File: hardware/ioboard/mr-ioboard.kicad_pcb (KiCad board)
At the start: 4 copper layers, 65 x 80 mm, 131 parts, among them J1 Conn_01x40_Shielded, J2 USB_C_Receptacle_USB2.0, J3 Conn_01x06, J4 Micro_SD_Card_Det, J5 Conn_01x04, J6 Conn_01x02, Q1 2N7002, SW1 SW_Push, U1 TPS62822, U10 F1C200S, U11 TPS54202DDC, U2 TPS56637, U3 TPD2E2U06, U4 DS90C363, U5 TPD2E2U06, U6 LD3985M28R_SOT23, U7 TPS62822, U8 FUSB302BMPX, U9 TPD2E2U06, Y1 24MHz

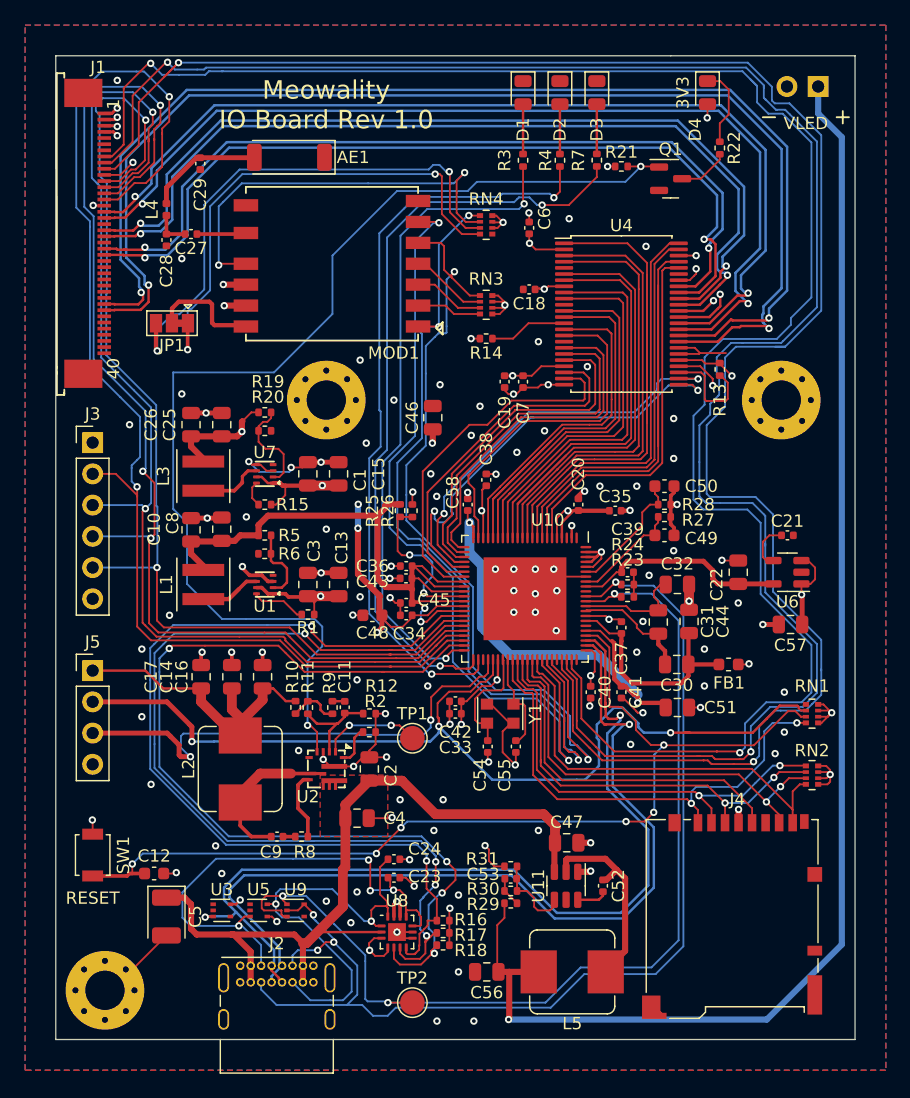
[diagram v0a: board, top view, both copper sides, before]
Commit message: Add LRADC buttons to IO board
Signed-off-by: gatecat <gatecat@ds0.me>
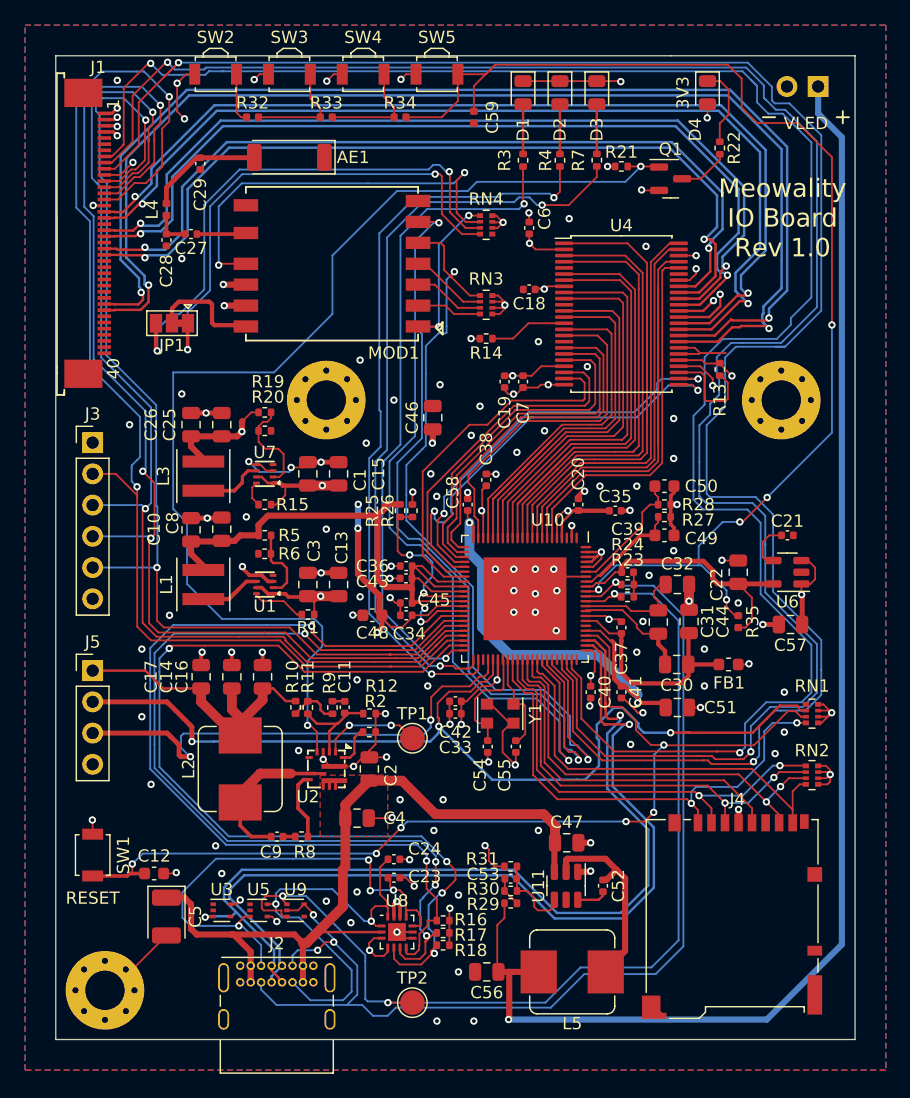
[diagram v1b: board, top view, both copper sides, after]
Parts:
- added C59: 100n, Capacitor_SMD:C_0402_1005Metric, F.Cu at (134.0, 55.0)
- added R32: 2.2k, Resistor_SMD:R_0402_1005Metric, F.Cu at (116.0, 55.0)
- added R33: 2.2k, Resistor_SMD:R_0402_1005Metric, F.Cu at (122.0, 55.0)
- added R34: 2.2k, Resistor_SMD:R_0402_1005Metric, F.Cu at (128.0, 55.0)
- added R35: 2.2k, Resistor_SMD:R_0402_1005Metric, F.Cu at (155.5, 96.0)
- added SW2: SW_Push, Button_Switch_SMD:SW_SPST_B3U-3000P, F.Cu at (113.0, 51.5)
- added SW3: SW_Push, Button_Switch_SMD:SW_SPST_B3U-3000P, F.Cu at (119.0, 51.5)
- added SW4: SW_Push, Button_Switch_SMD:SW_SPST_B3U-3000P, F.Cu at (125.0, 51.5)
- added SW5: SW_Push, Button_Switch_SMD:SW_SPST_B3U-3000P, F.Cu at (131.0, 51.5)
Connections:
- U10 pad 79: unconnected-(U10-Pad79) -> /LRADC
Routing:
- net /LRADC: track 0.00 -> 101.3 mm, vias 0 -> 5
- net GND: track 132.3 -> 150.8 mm, vias 121 -> 128
- net Net-(R33-Pad2): track 0.00 -> 8.87 mm
- net Net-(R32-Pad2): track 0.00 -> 8.87 mm
- net +2V8: track 17.5 -> 22.3 mm
- net Net-(R32-Pad1): track 0.00 -> 4.09 mm
- net /Vra1: track 8.78 -> 9.70 mm

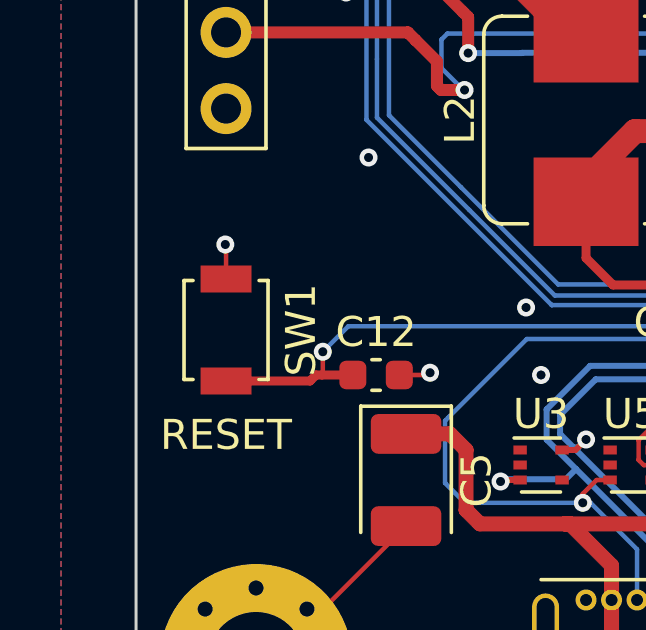
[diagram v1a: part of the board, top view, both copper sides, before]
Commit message: Use B3U-3000P for all buttons
Signed-off-by: gatecat <gatecat@ds0.me>
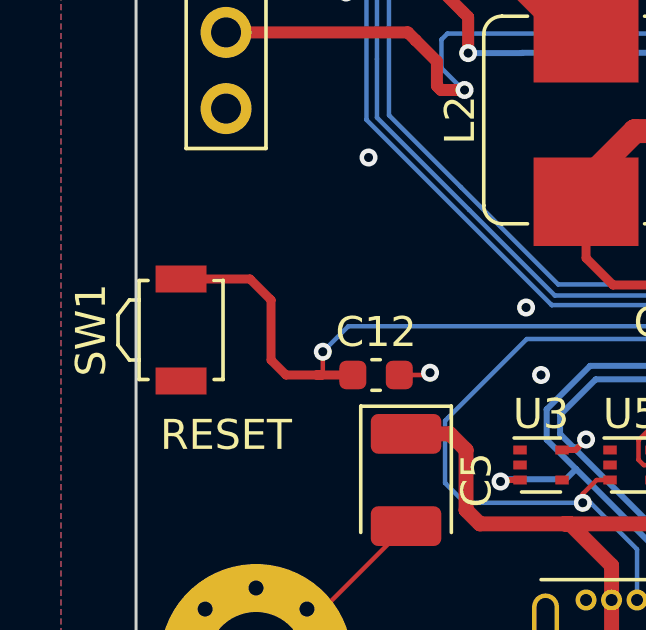
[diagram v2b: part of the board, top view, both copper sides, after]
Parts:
- SW1: footprint Button_Switch_SMD:SW_SPST_B3U-1000P -> Button_Switch_SMD:SW_SPST_B3U-3000P
- moved SW1 1.50 mm to (101.5, 115.0), turned to 90 degrees
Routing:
- net /RESET: track 81.3 -> 85.4 mm
- net GND: track 150.8 -> 149.6 mm, vias 128 -> 127
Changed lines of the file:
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@@
     (fp_line (start -0.85 -1.25) (end -0.85 -1.65) (layer "F.Fab") (width 0.1))
     (pad "1" smd rect (at -1.7 0) (locked) (size 0.9 1.7) (layers "F.Cu" "F.Paste" "F.Mask")
-      (net 2 "GND") (pinfunction "1"))
+      (net 2 "GND") (pinfunction "1") (pintype "passive"))
     (pad "2" smd rect (at 1.7 0) (locked) (size 0.9 1.7) (layers "F.Cu" "F.Paste" "F.Mask")
-      (net 126 "/LRADC") (pinfunction "2"))
+      (net 126 "/LRADC") (pinfunction "2") (pintype "passive"))
     (model "${KISYS3DMOD}/Button_Switch_SMD.3dshapes/SW_SPST_B3U-3000P.wrl"
       (offset (xyz 0 0 0))
@@
     )
   )
-  (footprint "Button_Switch_SMD:SW_SPST_B3U-1000P" (layer "F.Cu")
-    (at 103 115 -90)
-    (descr "Ultra-small-sized Tactile Switch with High Contact Reliability, Top-actuated Model, without Ground Terminal, without Boss")
+  (footprint "Button_Switch_SMD:SW_SPST_B3U-3000P" (layer "F.Cu")
+    (at 101.5 115 90)
+    (descr "Ultra-small-sized Tactile Switch with High Contact Reliability, Side-actuated Model, without Ground Terminal, without Boss")
     (tags "Tactile Switch")
     (property "Sheetfile" "mr-ioboard.kicad_sch")
     (property "Sheetname" "")
     (attr smd)
-    (fp_text reference "SW1" (at 0 -2.5 90) (layer "F.SilkS")
+    (fp_text reference "SW1" (at 0 -3 270) (layer "F.SilkS")
       (effects (font (size 1 1) (thickness 0.15)))
     )
-    (fp_text value "SW_Push" (at 0 2.5 90) (layer "F.Fab")
+    (fp_text value "SW_Push" (at 0 2.5 270) (layer "F.Fab")
       (effects (font (size 1 1) (thickness 0.15)))
     )
-    (fp_text user "${REFERENCE}" (at 0 -2.5 90) (layer "F.Fab")
+    (fp_text user "${REFERENCE}" (at 0 -3 270) (layer "F.Fab")
       (effects (font (size 1 1) (thickness 0.15)))
     )
-    (fp_line (start 1.65 1.4) (end 1.65 1.1) (layer "F.SilkS") (width 0.12))
-    (fp_line (start 1.65 -1.4) (end 1.65 -1.1) (layer "F.SilkS") (width 0.12))
-    (fp_line (start -1.65 -1.4) (end 1.65 -1.4) (layer "F.SilkS") (width 0.12))
     (fp_line (start -1.65 1.4) (end 1.65 1.4) (layer "F.SilkS") (width 0.12))
+    (fp_line (start -0.5 -2.1) (end 0.5 -2.1) (layer "F.SilkS") (width 0.12))
+    (fp_line (start -1 -1.72) (end -1 -1.4) (layer "F.SilkS") (width 0.12))
+    (fp_line (start 0.5 -2.1) (end 1 -1.72) (layer "F.SilkS") (width 0.12))
     (fp_line (start -1.65 -1.1) (end -1.65 -1.4) (layer "F.SilkS") (width 0.12))
+    (fp_line (start 1 -1.72) (end 1 -1.4) (layer "F.SilkS") (width 0.12))
+    (fp_line (start -0.5 -2.1) (end -1 -1.72) (layer "F.SilkS") (width 0.12))
     (fp_line (start -1.65 1.1) (end -1.65 1.4) (layer "F.SilkS") (width 0.12))
+    (fp_line (start 1.65 1.4) (end 1.65 1.1) (layer "F.SilkS") (width 0.12))
+    (fp_line (start -1.65 -1.4) (end 1.65 -1.4) (layer "F.SilkS") (width 0.12))
+    (fp_line (start 1.65 -1.4) (end 1.65 -1.1) (layer "F.SilkS") (width 0.12))
+    (fp_line (start 1.25 -1.65) (end 2.4 -1.65) (layer "F.CrtYd") (width 0.05))
+    (fp_line (start -2.4 1.65) (end 2.4 1.65) (layer "F.CrtYd") (width 0.05))
     (fp_line (start -2.4 -1.65) (end -2.4 1.65) (layer "F.CrtYd") (width 0.05))
-    (fp_line (start 2.4 -1.65) (end -2.4 -1.65) (layer "F.CrtYd") (width 0.05))
+    (fp_line (start -1.25 -2.35) (end 1.25 -2.35) (layer "F.CrtYd") (width 0.05))
+    (fp_line (start 1.25 -2.35) (end 1.25 -1.65) (layer "F.CrtYd") (width 0.05))
+    (fp_line (start -1.25 -1.65) (end -1.25 -2.35) (layer "F.CrtYd") (width 0.05))
     (fp_line (start 2.4 1.65) (end 2.4 -1.65) (layer "F.CrtYd") (width 0.05))
-    (fp_line (start -2.4 1.65) (end 2.4 1.65) (layer "F.CrtYd") (width 0.05))
+    (fp_line (start -1.25 -1.65) (end -2.4 -1.65) (layer "F.CrtYd") (width 0.05))
+    (fp_line (start 1.5 1.25) (end -1.5 1.25) (layer "F.Fab") (width 0.1))
+    (fp_line (start 0.45 -1.95) (end 0.85 -1.65) (layer "F.Fab") (width 0.1))
     (fp_line (start -1.5 1.25) (end -1.5 -1.25) (layer "F.Fab") (width 0.1))
-    (fp_line (start 1.5 -1.25) (end 1.5 1.25) (layer "F.Fab") (width 0.1))
+    (fp_line (start -0.85 -1.65) (end -0.45 -1.95) (layer "F.Fab") (width 0.1))
     (fp_line (start -1.5 -1.25) (end 1.5 -1.25) (layer "F.Fab") (width 0.1))
-    (fp_line (start 1.5 1.25) (end -1.5 1.25) (layer "F.Fab") (width 0.1))
-    (fp_circle (center 0 0) (end 0.75 0) (layer "F.Fab") (width 0.1) (fill none))
-    (pad "1" smd rect (at -1.7 0 270) (locked) (size 0.9 1.7) (layers "F.Cu" "F.Paste" "F.Mask")
+    (fp_line (start -0.85 -1.25) (end -0.85 -1.65) (layer "F.Fab") (width 0.1))
+    (fp_line (start 0.85 -1.65) (end 0.85 -1.25) (layer "F.Fab") (width 0.1))
+    (fp_line (start 1.5 -1.25) (end 1.5 1.25) (layer "F.Fab") (width 0.1))
+    (fp_line (start -0.45 -1.95) (end 0.45 -1.95) (layer "F.Fab") (width 0.1))
+    (pad "1" smd rect (at -1.7 0 90) (locked) (size 0.9 1.7) (layers "F.Cu" "F.Paste" "F.Mask")
       (net 2 "GND") (pinfunction "1") (pintype "passive"))
-    (pad "2" smd rect (at 1.7 0 270) (locked) (size 0.9 1.7) (layers "F.Cu" "F.Paste" "F.Mask")
+    (pad "2" smd rect (at 1.7 0 90) (locked) (size 0.9 1.7) (layers "F.Cu" "F.Paste" "F.Mask")
       (net 9 "/RESET") (pinfunction "2") (pintype "passive"))
-    (model "${KICAD6_3DMODEL_DIR}/Button_Switch_SMD.3dshapes/SW_SPST_B3U-1000P.wrl"
+    (model "${KISYS3DMOD}/Button_Switch_SMD.3dshapes/SW_SPST_B3U-3000P.wrl"
       (offset (xyz 0 0 0))
       (scale (xyz 1 1 1))
@@
   (segment (start 111.44 58.29) (end 111.75 58.29) (width 0.4) (layer "F.Cu") (net 1))
   (segment (start 111.82 98.58) (end 111.9 98.5) (width 0.3) (layer "F.Cu") (net 2))
-  (segment (start 103 113.3) (end 103 112.175) (width 0.15) (layer "F.Cu") (net 2))
   (segment (start 150.6625 68.25) (end 151.55 68.25) (width 0.15) (layer "F.Cu") (net 2))
   (segment (start 144.99 95.83) (end 145.81 95.83) (width 0.15) (layer "F.Cu") (net 2))
@@
   (segment (start 150.6625 74.25) (end 152.314292 74.25) (width 0.15) (layer "F.Cu") (net 2))
   (segment (start 139.45 76.75) (end 140.05 76.75) (width 0.15) (layer "F.Cu") (net 2))
-  (segment (start 103 112.175) (end 102.975 112.15) (width 0.15) (layer "F.Cu") (net 2))
   (segment (start 128 92.5) (end 127.17 92.5) (width 0.15) (layer "F.Cu") (net 2))
   (segment (start 144.37 90.89) (end 144.37 90.35) (width 0.15) (layer "F.Cu") (net 2))
@@
   (via (at 124.75 94) (size 0.6) (drill 0.3) (layers "F.Cu" "B.Cu") (net 2))
   (via (at 126.81 103.5) (size 0.6) (drill 0.3) (layers "F.Cu" "B.Cu") (net 2))
-  (via (at 102.975 112.15) (size 0.6) (drill 0.3) (layers "F.Cu" "B.Cu") (net 2))
   (via (at 139 95.25) (size 0.6) (drill 0.3) (layers "F.Cu" "B.Cu") (net 2))
   (via (at 150.25 82.75) (size 0.6) (drill 0.3) (layers "F.Cu" "B.Cu") (net 2))
@@
   (segment (start 122.5 102.49) (end 123.49 102.49) (width 0.2) (layer "F.Cu") (net 8))
   (segment (start 123.49 102.49) (end 123.5 102.5) (width 0.2) (layer "F.Cu") (net 8))
+  (segment (start 106.2 116.5) (end 105 116.5) (width 0.3) (layer "F.Cu") (net 9))
   (segment (start 149.6 106.075) (end 156.775 106.075) (width 0.15) (layer "F.Cu") (net 9))
   (segment (start 149.475 106.075) (end 149.45 106.05) (width 0.15) (layer "F.Cu") (net 9))
@@
   (segment (start 147.175 104.122189) (end 147.175 104.825) (width 0.15) (layer "F.Cu") (net 9))
   (segment (start 106.225 115.725) (end 106.225 116.475) (width 0.15) (layer "F.Cu") (net 9))
-  (segment (start 105.8 116.7) (end 106 116.5) (width 0.3) (layer "F.Cu") (net 9))
-  (segment (start 103 116.7) (end 105.8 116.7) (width 0.3) (layer "F.Cu") (net 9))
   (segment (start 145.775 102.95) (end 146.002811 102.95) (width 0.15) (layer "F.Cu") (net 9))
   (segment (start 148.4 106.05) (end 149.45 106.05) (width 0.15) (layer "F.Cu") (net 9))
   (segment (start 149.6 106.075) (end 149.475 106.075) (width 0.15) (layer "F.Cu") (net 9))
   (segment (start 144.0475 97.1575) (end 145.01998 98.12998) (width 0.15) (layer "F.Cu") (net 9))
+  (segment (start 104.5 114) (end 103.8 113.3) (width 0.3) (layer "F.Cu") (net 9))
+  (segment (start 105 116.5) (end 104.5 116) (width 0.3) (layer "F.Cu") (net 9))
   (segment (start 106.225 116.475) (end 106.2 116.5) (width 0.15) (layer "F.Cu") (net 9))
   (segment (start 126.075 114.775) (end 126.075 114.875) (width 0.15) (layer "F.Cu") (net 9))
   (segment (start 160.6 103.75) (end 161 103.75) (width 0.15) (layer "F.Cu") (net 9))
+  (segment (start 104.5 116) (end 104.5 114) (width 0.3) (layer "F.Cu") (net 9))
+  (segment (start 103.8 113.3) (end 101.5 113.3) (width 0.3) (layer "F.Cu") (net 9))
   (segment (start 159.55 103.3) (end 160.15 103.3) (width 0.15) (layer "F.Cu") (net 9))
   (segment (start 147.175 104.825) (end 148.4 106.05) (width 0.15) (layer "F.Cu") (net 9))
